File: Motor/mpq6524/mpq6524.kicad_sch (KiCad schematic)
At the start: 11 parts, among them J1 OQ0212500000G, J2 Conn_02x03_Odd_Even, U1 MPQ6524GRE-AEC1-P, U2 TPS5410DR

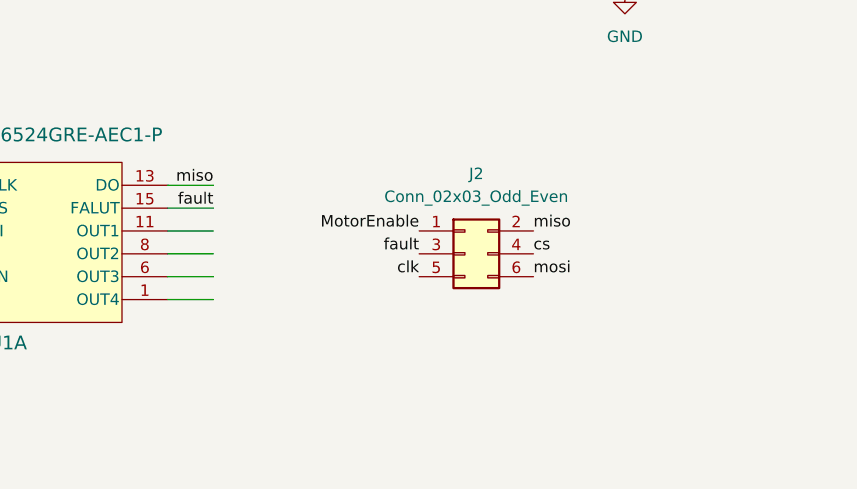
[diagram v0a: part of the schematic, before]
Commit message: Motor connector
Add motor connector
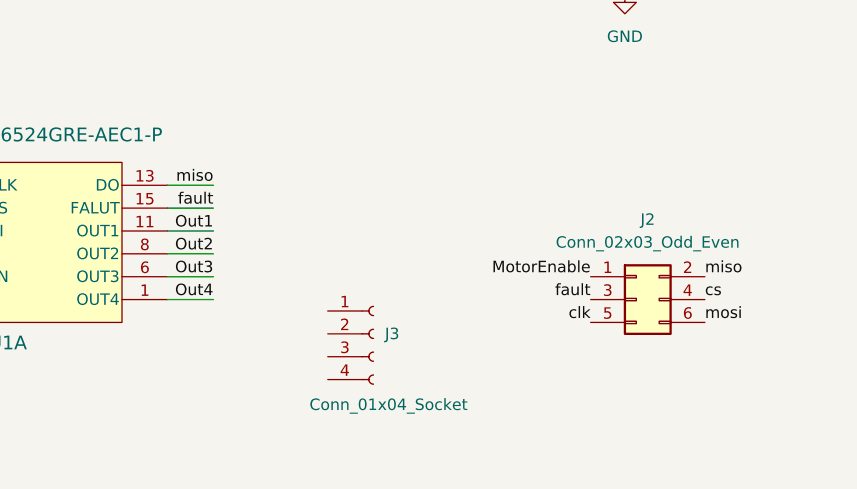
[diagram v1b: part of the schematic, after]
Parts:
- added J3: Conn_01x04_Socket, Connector_Molex:Molex_SL_171971-0004_1x04_P2.54mm_Vertical, symbol Connector:Conn_01x04_Socket
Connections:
- net Out4: now reaches U1.1 (OUT4)
- net Out1: now reaches U1.11 (OUT1)
- net Out3: now reaches U1.6 (OUT3)
- net Out2: now reaches U1.8 (OUT2)
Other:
- moved on the sheet: J2

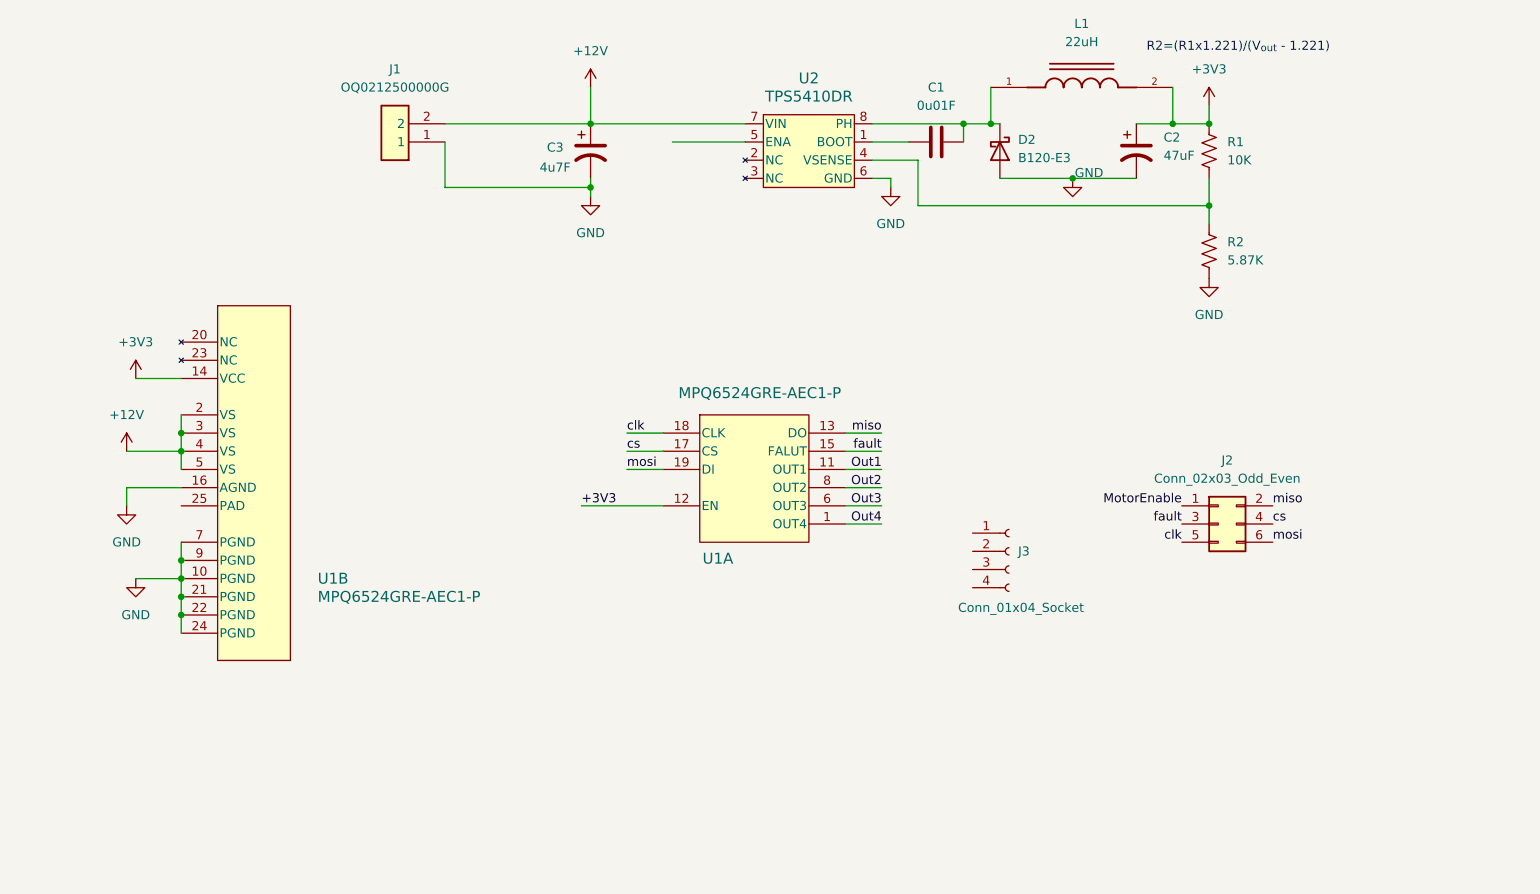
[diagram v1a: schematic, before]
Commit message: Motor connector
added smd connector for the motor outputs
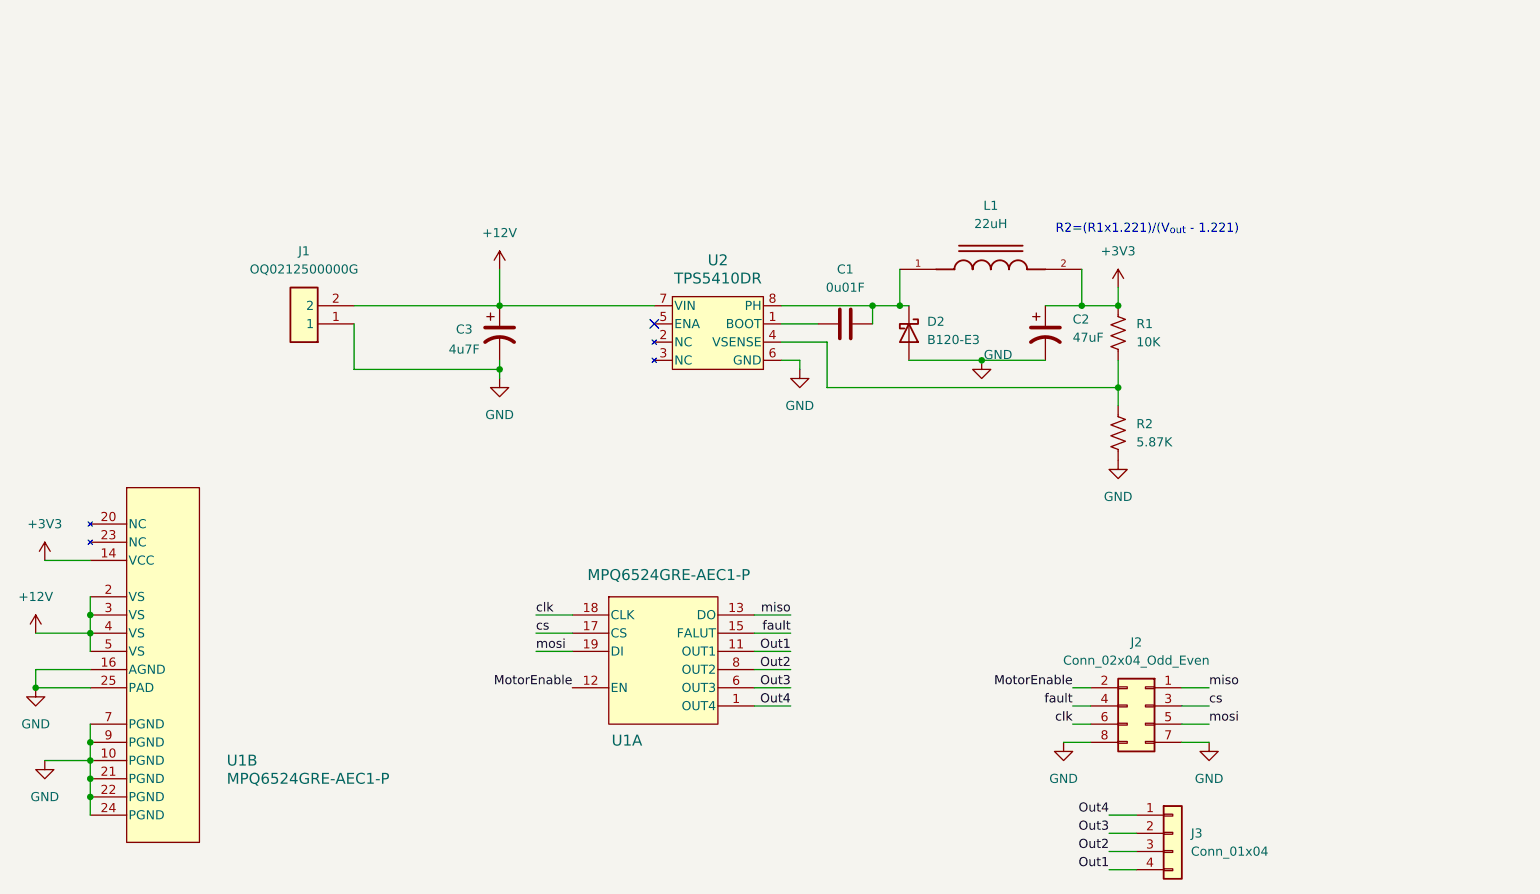
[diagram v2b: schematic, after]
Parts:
- removed J2: Conn_02x03_Odd_Even, Connector_PinHeader_2.54mm:PinHeader_2x03_P2.54mm_Vertical_SMD, symbol Connector_Generic:Conn_02x03_Odd_Even
- removed J3: Conn_01x04_Socket, Connector_Molex:Molex_SL_171971-0004_1x04_P2.54mm_Vertical, symbol Connector:Conn_01x04_Socket
- added J2: Conn_02x04_Odd_Even, Connector_PinSocket_2.54mm:PinSocket_2x04_P2.54mm_Vertical_SMD, symbol Connector_Generic:Conn_02x04_Odd_Even
- added J3: Conn_01x04, Connector_PinSocket_2.54mm:PinSocket_1x04_P2.54mm_Vertical_SMD_Pin1Left, symbol Connector_Generic:Conn_01x04
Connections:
- net +3V3: no longer U1.12 (EN)
- net GND: now also U1.25 (PAD), J2.7 (Pin_7), J2.8 (Pin_8)
- net MotorEnable: now also U1.12 (EN), J2.2 (Pin_2)
- net Out1: now also J3.4 (Pin_4)
- net Out2: now also J3.3 (Pin_3)
- net Out3: now also J3.2 (Pin_2)
- net Out4: now also J3.1 (Pin_1)
- net clk: now also J2.6 (Pin_6)
- net cs: now also J2.3 (Pin_3)
- net fault: now also J2.4 (Pin_4)
- net miso: now also J2.1 (Pin_1)
- net mosi: now also J2.5 (Pin_5)
- no-connect marks 0 -> 1
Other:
- moved on the sheet: C1, C2, C3, D2, J1, L1, R1, R2, U1A, U1B, U2

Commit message: footprints
Update capacitor footprints
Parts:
- C2: footprint Capacitor_Tantalum_SMD:CP_EIA-3528-21_Kemet-B_HandSolder -> Capacitor_Tantalum_SMD:CP_EIA-3216-10_Kemet-I_HandSolder
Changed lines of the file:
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@@
 			)
 		)
-		(property "Footprint" "Capacitor_Tantalum_SMD:CP_EIA-3528-21_Kemet-B_HandSolder"
+		(property "Footprint" "Capacitor_Tantalum_SMD:CP_EIA-3216-10_Kemet-I_HandSolder"
 			(at 198.12 60.96 0)
 			(effects

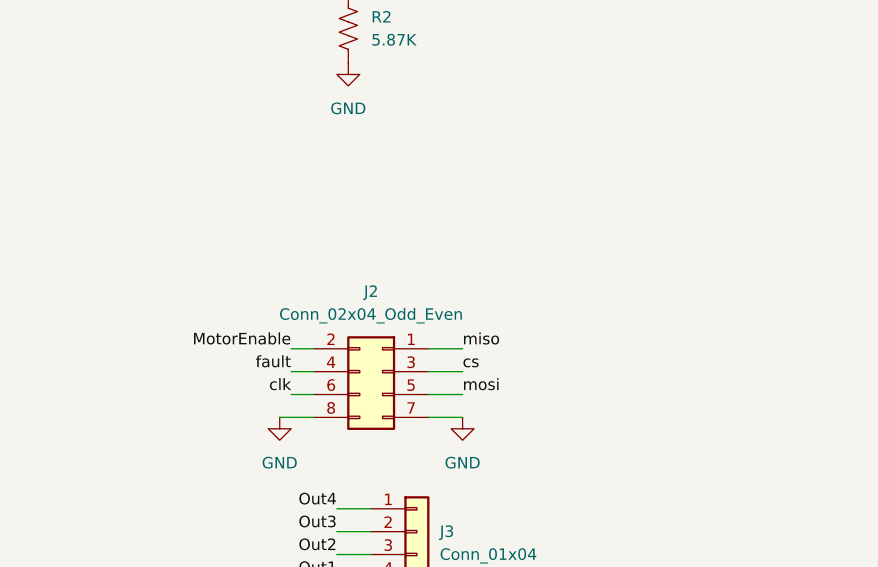
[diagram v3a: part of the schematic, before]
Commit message: Layout
Update layouts for the motor drivers
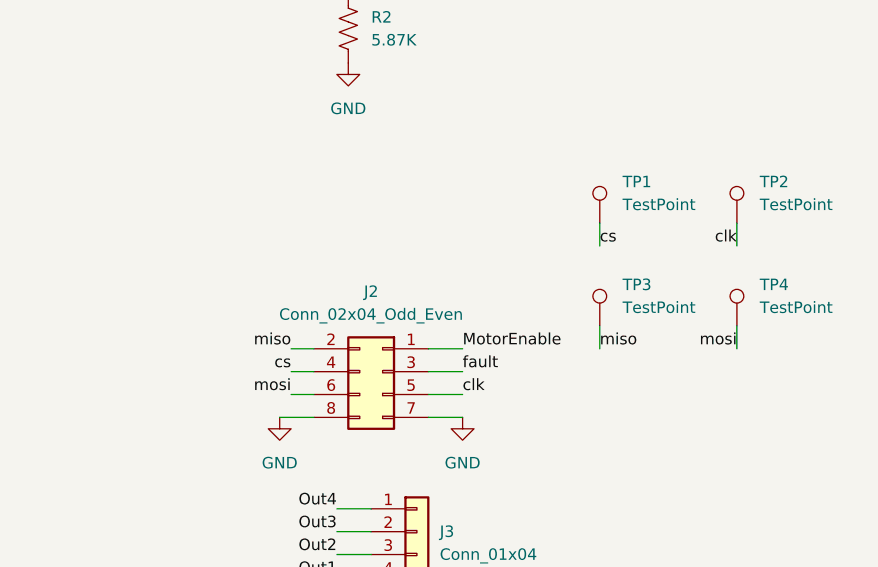
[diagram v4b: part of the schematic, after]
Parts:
- added TP1, TP2, TP3, TP4: TestPoint, TestPoint:TestPoint_Loop_D1.80mm_Drill1.0mm_Beaded, symbol Connector:TestPoint
- J2: footprint Connector_PinSocket_2.54mm:PinSocket_2x04_P2.54mm_Vertical_SMD -> Connector_PinHeader_2.54mm:PinHeader_2x04_P2.54mm_Vertical
- J3: footprint Connector_PinSocket_2.54mm:PinSocket_1x04_P2.54mm_Vertical_SMD_Pin1Left -> Connector_PinHeader_2.54mm:PinHeader_1x04_P2.54mm_Vertical
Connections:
- net MotorEnable: now also J2.1 (Pin_1); no longer J2.2 (Pin_2)
- net clk: now also J2.5 (Pin_5), TP2.1; no longer J2.6 (Pin_6)
- net cs: now also J2.4 (Pin_4), TP1.1; no longer J2.3 (Pin_3)
- net fault: now also J2.3 (Pin_3); no longer J2.4 (Pin_4)
- net miso: now also J2.2 (Pin_2), TP3.1; no longer J2.1 (Pin_1)
- net mosi: now also J2.6 (Pin_6), TP4.1; no longer J2.5 (Pin_5)
